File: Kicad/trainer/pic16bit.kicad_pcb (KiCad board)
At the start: 2 copper layers, 160 x 100 mm, 123 parts, among them K101 AC/DC 9-12V, K102 AC/DC 9-12V, K103 PE-450-4X6X-BLACK, K201 MCU 1, K202 MCU 2, K203 ICSP, K204 VIN, K205 VIN, K206 VDD, K207 GND, K208 VDD, K209 GND, K210 HARWIN-254-F-1X10-VERTICAL, K301 I2C/GPIO, K303 SPI/GPIO, K304 EUSART/TTL, K401 HARWIN-254-F-1X10-VERTICAL, K402 HARWIN-254-F-1X10-VERTICAL, K409 HARWIN-254-F-1X16-VERTICAL, P401 AN1, P402 AN2, U101 KEYSTONE-24283, U102 KEYSTONE-24283, U103 KEYSTONE-24283, U104 KEYSTONE-24283, U105 NCP5662-ADJ, U201 PIC24/dsPIC33, X101 3M-SJ5376, X102 3M-SJ5376, X103 3M-SJ5376, X104 3M-SJ5376, X105 3M-SJ5376, X201 XTAL-DIL08

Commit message: Update
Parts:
- C101, C102: footprint tronixio:CAPACITOR-ELECTROLYTIC-RADIAL-080-110-035 -> tronixio:CAPACITOR-ELECTROLYTIC-RADIAL-080-115-035

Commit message: Update
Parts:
- R401: footprint tronixio:PIHER-PT10LV -> tronixio:PIHER-PT10MV
- U101, U102, U103, U104: value KEYSTONE-24283 -> 24283
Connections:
- net VDD renamed +VDD
- net VIN renamed +VIN
- S403 pad 4: GND -> /HID/S5
- S403 pad 5: /HID/S5 -> GND
- X201 pad 2: GND -> unconnected-(X201-Pad2)
- X201 pad 4: Net-(K201-Pin_9) -> unconnected-(X201-Pad4)
- X201 pad 6: Net-(K201-Pin_10) -> unconnected-(X201-Pad6)
- X201 pad 7: GND -> unconnected-(X201-Pad7)
- X201 pad 8: GND -> unconnected-(X201-Pad8)

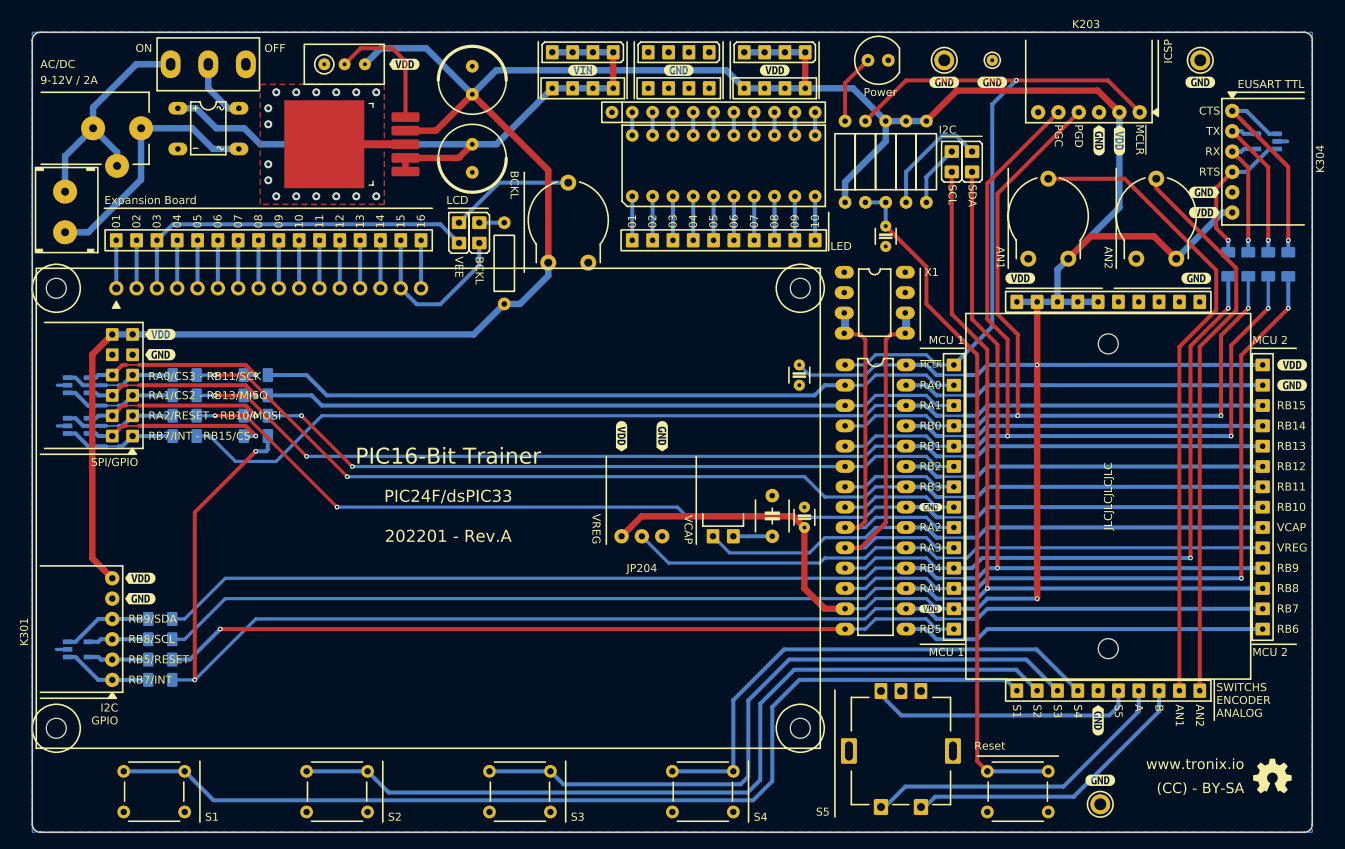
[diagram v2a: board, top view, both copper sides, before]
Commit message: Update Trainer Kicad 8
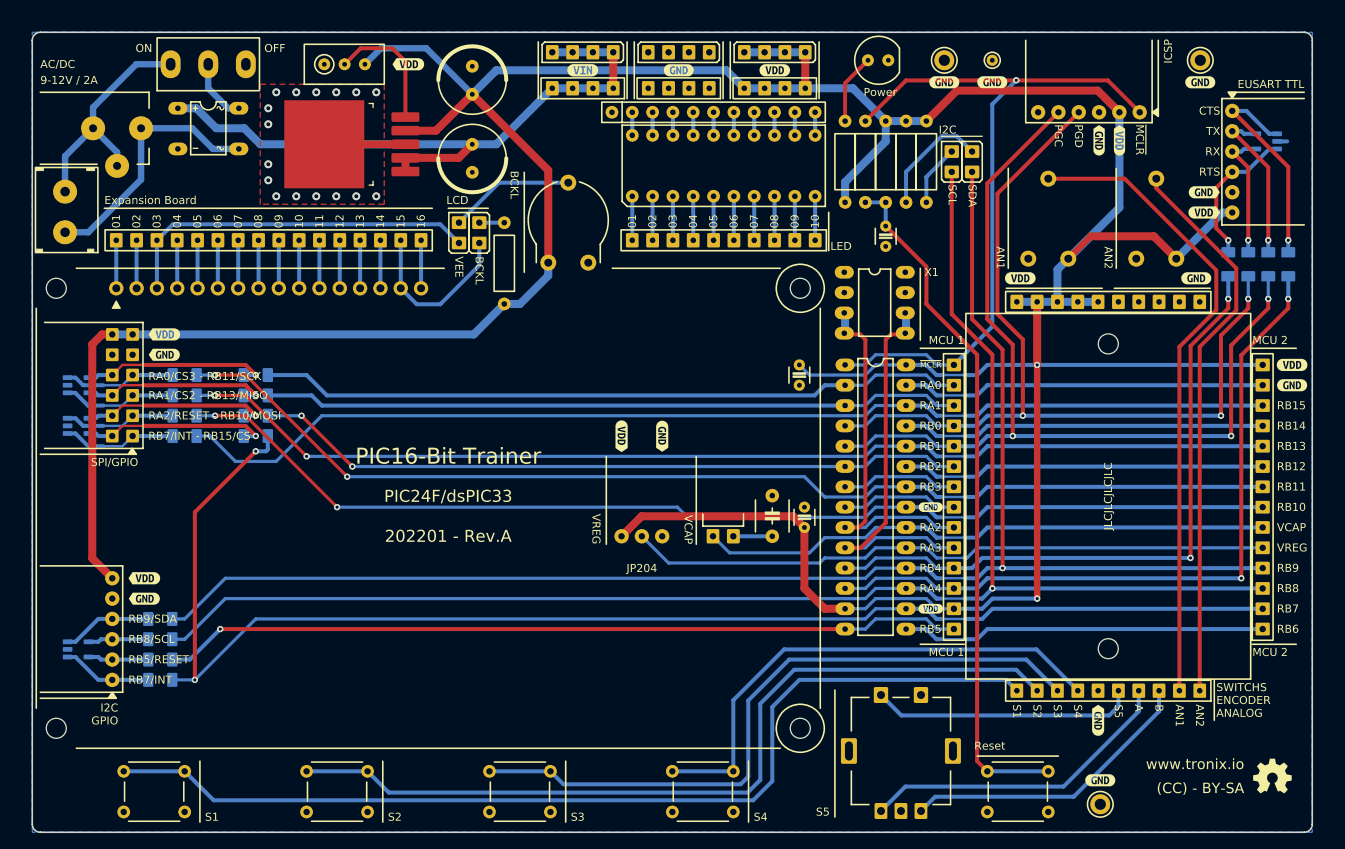
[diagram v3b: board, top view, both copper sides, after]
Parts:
- removed kibuzzard-62A777FA (x7): G***, kibuzzard-62A777FA
- removed kibuzzard-62A77857: G***, kibuzzard-62A77857
- removed the kibuzzard-62A778D1 at (200.2, 133.0)
- removed kibuzzard-62A77FCE: G***, kibuzzard-62A77FCE
- removed kibuzzard-62A77FF4: G***, kibuzzard-62A77FF4
- removed kibuzzard-62A78037: G***, kibuzzard-62A78037
- removed kibuzzard-62A78078: G***, kibuzzard-62A78078
- removed kibuzzard-62A780A0 (x2): G***, kibuzzard-62A780A0
- removed kibuzzard-62A780B6: G***, kibuzzard-62A780B6
- removed kibuzzard-62AA3F24: G***, kibuzzard-62AA3F24
- removed kibuzzard-62ACBAD0: G***, kibuzzard-62ACBAD0
- removed kibuzzard-62ACDA78: G***, kibuzzard-62ACDA78
- removed kibuzzard-6313AD44: G***, kibuzzard-6313AD44
- removed kibuzzard-6313AD54: G***, kibuzzard-6313AD54
- removed kibuzzard-6313AEE5: G***, kibuzzard-6313AEE5
- removed kibuzzard-6313AEF3: G***, kibuzzard-6313AEF3
- added kibuzzard-65F6F3C0: G***, kibuzzard-65F6F3C0, F.Cu at (114.0, 51.0)
- added kibuzzard-65F6F3D4: G***, kibuzzard-65F6F3D4, F.Cu at (135.8, 51.8)
- added kibuzzard-65F6F3E0: G***, kibuzzard-65F6F3E0, F.Cu at (147.8, 51.8)
- added kibuzzard-65F6F3EC: G***, kibuzzard-65F6F3EC, F.Cu at (159.8, 51.8)
- added kibuzzard-65F6F3F9: G***, kibuzzard-65F6F3F9, F.Cu at (181.0, 53.2)
- added kibuzzard-65F6F405: G***, kibuzzard-65F6F405, F.Cu at (187.0, 53.2)
- added kibuzzard-65F6F414: G***, kibuzzard-65F6F414, F.Cu at (213.0, 53.2)
- added kibuzzard-65F6F420: G***, kibuzzard-65F6F420, F.Cu at (213.5, 67.0)
- added kibuzzard-65F6F42E: G***, kibuzzard-65F6F42E, F.Cu at (213.5, 69.5)
- added kibuzzard-65F6F438: G***, kibuzzard-65F6F438, F.Cu at (212.5, 77.8)
- added kibuzzard-65F6F442: G***, kibuzzard-65F6F442, F.Cu at (190.5, 77.8)
- added kibuzzard-65F6F450: G***, kibuzzard-65F6F450, F.Cu at (224.5, 88.6)
- added kibuzzard-65F6F45D: G***, kibuzzard-65F6F45D, F.Cu at (224.5, 91.1)
- added kibuzzard-65F6F46A: G***, kibuzzard-65F6F46A, F.Cu at (179.3, 106.4)
- added kibuzzard-65F6F480: G***, kibuzzard-65F6F480, F.Cu at (179.3, 119.1)
- added kibuzzard-65F6F48D: G***, kibuzzard-65F6F48D, F.Cu at (200.2, 133.0)
- added kibuzzard-65F6F499: G***, kibuzzard-65F6F499, F.Cu at (200.5, 140.5)
- added kibuzzard-65F6F4AB: G***, kibuzzard-65F6F4AB, F.Cu at (145.7, 97.5)
- added kibuzzard-65F6F4B8: G***, kibuzzard-65F6F4B8, F.Cu at (140.7, 97.5)
- added kibuzzard-65F6F4C9: G***, kibuzzard-65F6F4C9, F.Cu at (81.0, 117.8)
- added kibuzzard-65F6F4DA: G***, kibuzzard-65F6F4DA, F.Cu at (81.0, 115.2)
- added kibuzzard-65F6F4F1: G***, kibuzzard-65F6F4F1, F.Cu at (83.5, 87.3)
- added kibuzzard-65F6F500: G***, kibuzzard-65F6F500, F.Cu at (83.5, 84.8)
- LED101: footprint tronixio:LED-TH-05MM -> tronixio:LED-TH-ROUND-05MM
- U101, U102, U103, U104: value 24283 -> KEYSTONE-24283
- turned S403 to 180 degrees
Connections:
- net +VDD renamed POWER-VDD
- net +VIN renamed POWER-VIN
- B101 pad 2: GND -> POWER-GND
- C101 pad 2: GND -> POWER-GND
- C102 pad 2: GND -> POWER-GND
- C201 pad 2: GND -> POWER-GND
- C202 pad 2: GND -> POWER-GND
- C203 pad 2: GND -> POWER-GND
- C204 pad 2: GND -> POWER-GND
- D301 pad 2: GND -> POWER-GND
- D302 pad 2: GND -> POWER-GND
- D303 pad 2: GND -> POWER-GND
- D304 pad 2: GND -> POWER-GND
- JP204 pad 3: GND -> POWER-GND
- K201 pad 8: GND -> POWER-GND
- K202 pad 2: GND -> POWER-GND
- K203 pad 4: GND -> POWER-GND
- K207 pad 1: GND -> POWER-GND
- K207 pad 2: GND -> POWER-GND
- K207 pad 3: GND -> POWER-GND
- K207 pad 4: GND -> POWER-GND
- K209 pad 1: GND -> POWER-GND
- K209 pad 2: GND -> POWER-GND
- K209 pad 3: GND -> POWER-GND
- K209 pad 4: GND -> POWER-GND
- K210 pad 10: GND -> POWER-GND
- K210 pad 6: GND -> POWER-GND
- K210 pad 7: GND -> POWER-GND
- K210 pad 8: GND -> POWER-GND
- K210 pad 9: GND -> POWER-GND
- K301 pad 5: GND -> POWER-GND
- K303 pad 10: GND -> POWER-GND
- K303 pad 9: GND -> POWER-GND
- K304 pad 5: GND -> POWER-GND
- K402 pad 5: GND -> POWER-GND
- LED101 pad 1: GND -> POWER-GND
- P401 pad 1: GND -> POWER-GND
- P402 pad 1: GND -> POWER-GND
- R101 pad 1: GND -> POWER-GND
- R401 pad 3: GND -> POWER-GND
- RA401 pad 1: GND -> POWER-GND
- S201 pad 3: GND -> POWER-GND
- S201 pad 4: GND -> POWER-GND
- S401 pad 3: GND -> POWER-GND
- S401 pad 4: GND -> POWER-GND
- S402 pad 3: GND -> POWER-GND
- S402 pad 4: GND -> POWER-GND
- S403 pad 2: GND -> POWER-GND
- S403 pad 5: GND -> POWER-GND
- S404 pad 3: GND -> POWER-GND
- S404 pad 4: GND -> POWER-GND
- S405 pad 3: GND -> POWER-GND
- S405 pad 4: GND -> POWER-GND
- TP101 pad 1: GND -> POWER-GND
- TP102 pad 1: GND -> POWER-GND
- TP103 pad 1: GND -> POWER-GND
- TP104 pad 1: GND -> POWER-GND
- U105 pad 3: GND -> POWER-GND
- U201 pad 27: GND -> POWER-GND
- U201 pad 8: GND -> POWER-GND
- X201 pad 1: GND -> POWER-GND
- X201 pad 2: unconnected-(X201-Pad2) -> POWER-GND
- X201 pad 4: unconnected-(X201-Pad4) -> Net-(K201-Pin_9)
- X201 pad 6: unconnected-(X201-Pad6) -> Net-(K201-Pin_10)
- X201 pad 7: unconnected-(X201-Pad7) -> POWER-GND
- X201 pad 8: unconnected-(X201-Pad8) -> POWER-GND
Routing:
- net GND: track 75.7 -> 0.00 mm, vias 16 -> 0
- net POWER-GND: track 0.00 -> 71.7 mm, vias 0 -> 16
- net POWER-VDD: track 478.6 -> 479.4 mm
- added copper zone on B.Cu, net POWER-GND
- added copper zone on F.Cu, net POWER-GND
- removed copper zone on B.Cu, net GND
- removed copper zone on F.Cu, net GND
